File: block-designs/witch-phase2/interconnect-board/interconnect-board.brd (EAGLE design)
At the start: 142.2 x 71.1 mm, 10 parts

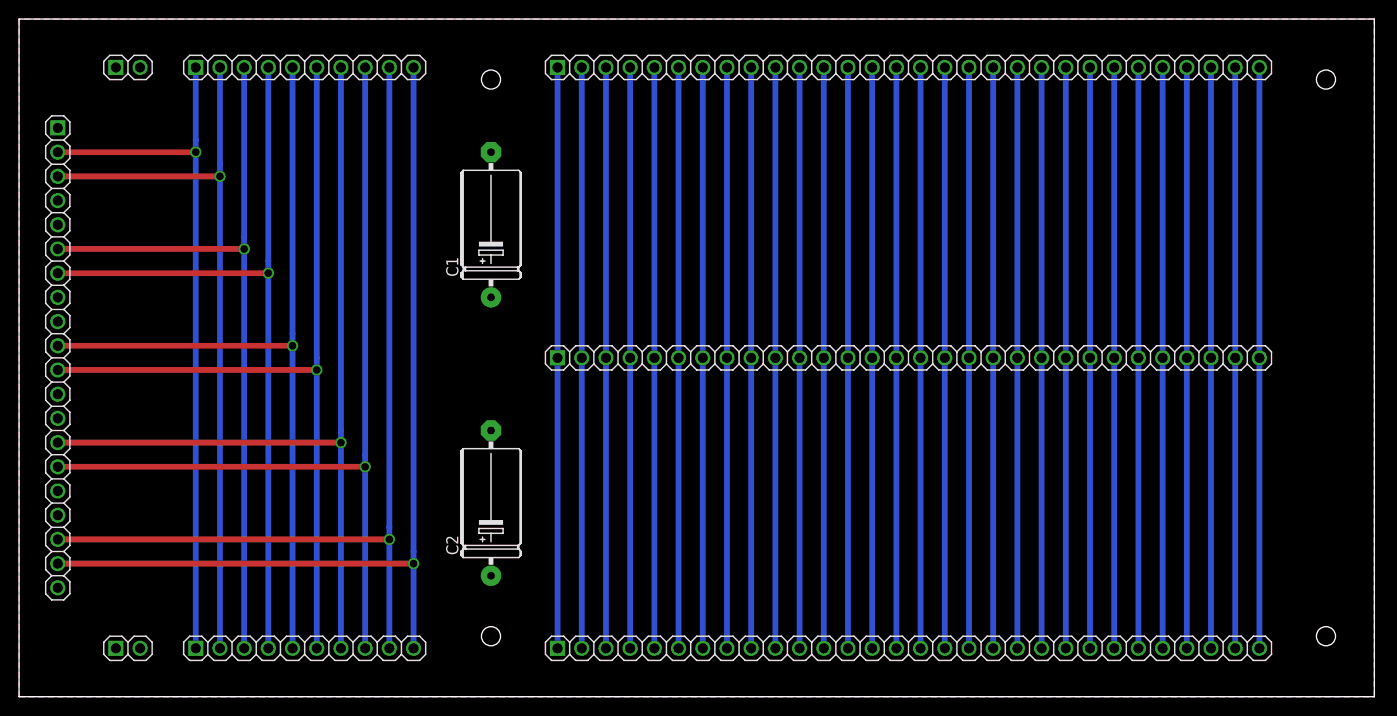
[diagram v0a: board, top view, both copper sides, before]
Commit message: update the interconnect board with spacing and layout changes
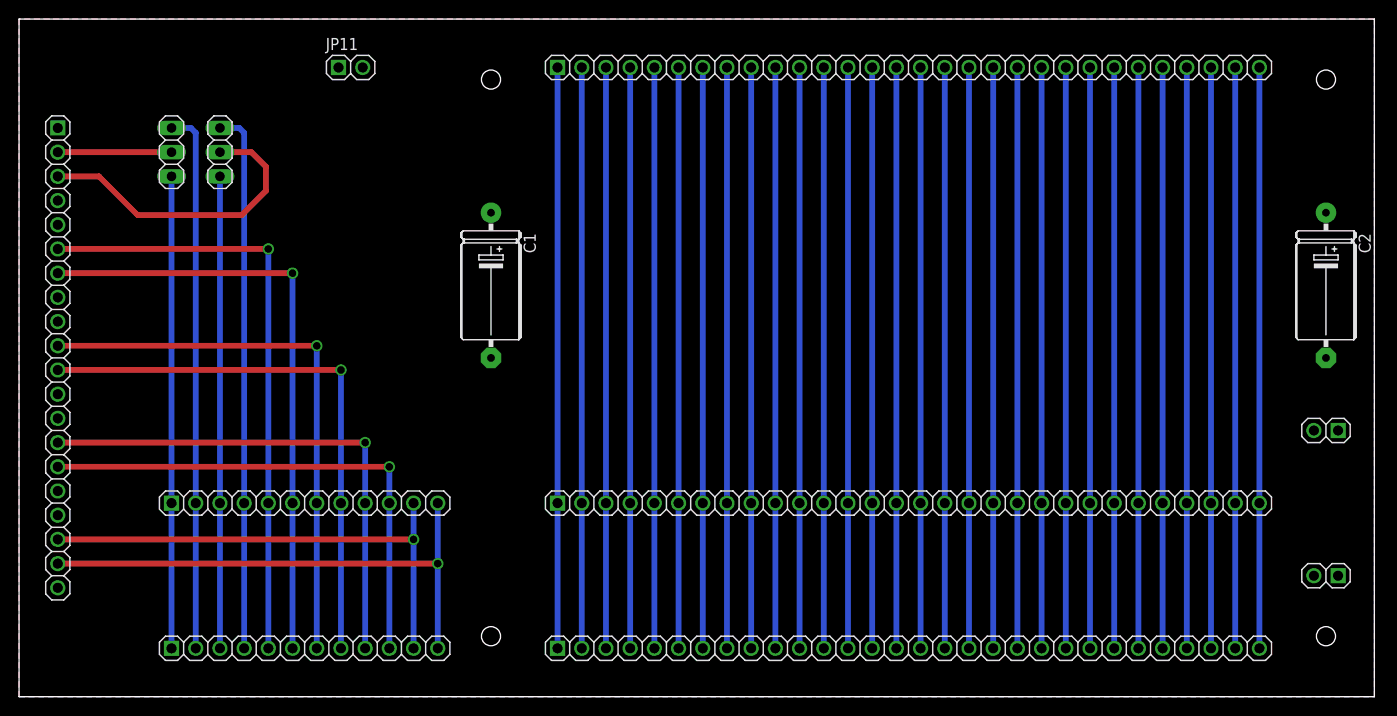
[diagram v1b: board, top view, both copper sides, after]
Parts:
- added JP10: (no value), pinhead:1X03
- added JP11: (no value), pinhead:1X02
- added JP9: (no value), pinhead:1X12
- JP2: device pinhead:1X10 -> pinhead:1X12
- JP3: device pinhead:1X10 -> pinhead:1X03
- moved JP7 136.6 mm to (137.2, 12.7), turned to 180 degrees
- moved JP8 127.8 mm to (137.2, 27.9), turned to 180 degrees
- moved C2 90.6 mm to (137.2, 43.2), turned to 270 degrees
- moved JP6 15.2 mm to (93.3, 20.3)
- moved JP3 12.6 mm to (21.1, 57.1), turned to 270 degrees
- moved C1 6.35 mm to (49.5, 43.2), turned to 270 degrees
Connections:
- new net N$41: JP10.1, JP2.2, JP9.2
- new net N$43: JP1.3, JP3.2
- new net N$44: JP1.2, JP10.2
- new net N$46: JP10.3, JP2.1, JP9.1
- net GND: now also JP11.2
- net N$31: now also JP2.12, JP9.12; no longer JP2.10, JP3.10
- net N$32: now also JP2.11, JP9.11; no longer JP2.9, JP3.9
- net N$33: now also JP2.10, JP9.10; no longer JP2.8, JP3.8
- net N$34: now also JP2.9, JP9.9; no longer JP2.7, JP3.7
- net N$35: now also JP2.8, JP9.8; no longer JP2.6, JP3.6
- net N$36: now also JP2.7, JP9.7; no longer JP2.5, JP3.5
- net N$37: now also JP2.6, JP9.6; no longer JP2.4, JP3.4
- net N$38: now also JP2.5, JP9.5; no longer JP2.3, JP3.3
- net N$39: now also JP2.4, JP3.1, JP9.4; no longer JP1.3, JP2.2, JP3.2
- net N$40: now also JP2.3, JP3.3, JP9.3; no longer JP1.2, JP2.1, JP3.1
- net VCC: now also JP11.1
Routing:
- net N$41: track 0.00 -> 56.9 mm
- net N$46: track 0.00 -> 49.5 mm
- net N$32: track 95.8 -> 52.6 mm
- net N$31: track 98.3 -> 55.1 mm
- net N$33: track 93.2 -> 53.8 mm
- net N$34: track 90.7 -> 53.8 mm
- net N$43: track 0.00 -> 32.6 mm
- net N$35: track 88.1 -> 58.9 mm
- net N$36: track 85.6 -> 58.9 mm
- net N$40: track 75.4 -> 49.5 mm, vias 1 -> 0
- net N$39: track 78.0 -> 56.9 mm, vias 1 -> 0
- net N$37: track 83.1 -> 64.0 mm
- net N$38: track 80.5 -> 64.0 mm
- net N$44: track 0.00 -> 11.9 mm
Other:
- board text removed: "1"
- board text removed: "10"
- board text removed: "20"
- board text removed: "30"

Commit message: updated design for layout for use with dupont connectors
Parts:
- added JP12: (no value), pinhead:1X02
- moved JP11 67.7 mm to (5.33, 5.08)
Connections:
- net GND: now also JP12.2
- net VCC: now also JP12.1
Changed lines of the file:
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@@
 <text x="109.982" y="12.446" size="1.778" layer="48" rot="SR180">Mini-Store Interconnect Board</text>
 <text x="107.442" y="16.002" size="1.778" layer="48" rot="SR180">http://www.witch-e.org</text>
-<text x="32.766" y="62.992" size="2.1844" layer="48">+</text>
-<text x="35.56" y="62.992" size="2.1844" layer="48">-</text>
+<text x="3.302" y="2.032" size="2.1844" layer="48">+</text>
+<text x="6.096" y="2.032" size="2.1844" layer="48">-</text>
+<text x="3.048" y="67.564" size="2.1844" layer="48">+</text>
+<text x="5.842" y="67.564" size="2.1844" layer="48">-</text>
 </plain>
 <attributes>
@@
 <attribute name="VALUE" x="139.7" y="31.115" size="1.27" layer="27" rot="R180"/>
 </element>
-<element name="C1" library="resistor" package="E15-6" value="" x="49.53" y="43.18" rot="R270"/>
-<element name="C2" library="resistor" package="E15-6" value="" x="137.16" y="43.18" rot="R270"/>
+<element name="C1" library="resistor" package="E15-6" value="" x="49.53" y="43.18" smashed="yes" rot="R270">
+<attribute name="VALUE" x="47.6758" y="43.815" size="1.27" layer="27" ratio="10" rot="R270"/>
+</element>
+<element name="C2" library="resistor" package="E15-6" value="" x="137.16" y="43.18" smashed="yes" rot="R270">
+<attribute name="VALUE" x="135.3058" y="43.815" size="1.27" layer="27" ratio="10" rot="R270"/>
+</element>
 <element name="JP9" library="pinhead" package="1X12" value="" x="29.972" y="20.32" smashed="yes">
 <attribute name="VALUE" x="14.732" y="17.145" size="1.27" layer="27"/>
@@
 <attribute name="VALUE" x="12.827" y="60.96" size="1.27" layer="27" rot="R270"/>
 </element>
-<element name="JP11" library="pinhead" package="1X02" value="" x="34.798" y="66.04"/>
+<element name="JP11" library="pinhead" package="1X02" value="" x="5.334" y="5.08" smashed="yes">
+<attribute name="VALUE" x="2.794" y="1.905" size="1.27" layer="27"/>
+</element>
+<element name="JP12" library="pinhead" package="1X02" value="" x="5.334" y="66.04" smashed="yes">
+<attribute name="VALUE" x="2.794" y="62.865" size="1.27" layer="27"/>
+</element>
 </elements>
 <signals>
@@
 <contactref element="C1" pad="-"/>
 <contactref element="JP11" pad="2"/>
+<contactref element="JP12" pad="2"/>
 </signal>
 <signal name="VCC">
@@
 <contactref element="C1" pad="+"/>
 <contactref element="JP11" pad="1"/>
+<contactref element="JP12" pad="1"/>
 </signal>
 <signal name="N$31">
